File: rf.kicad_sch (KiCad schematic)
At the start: 57 parts, among them Q1 2N7002, U12 SN74AUP1G17, U13 ST25R3916B-AQET, Y3 27.12MHz

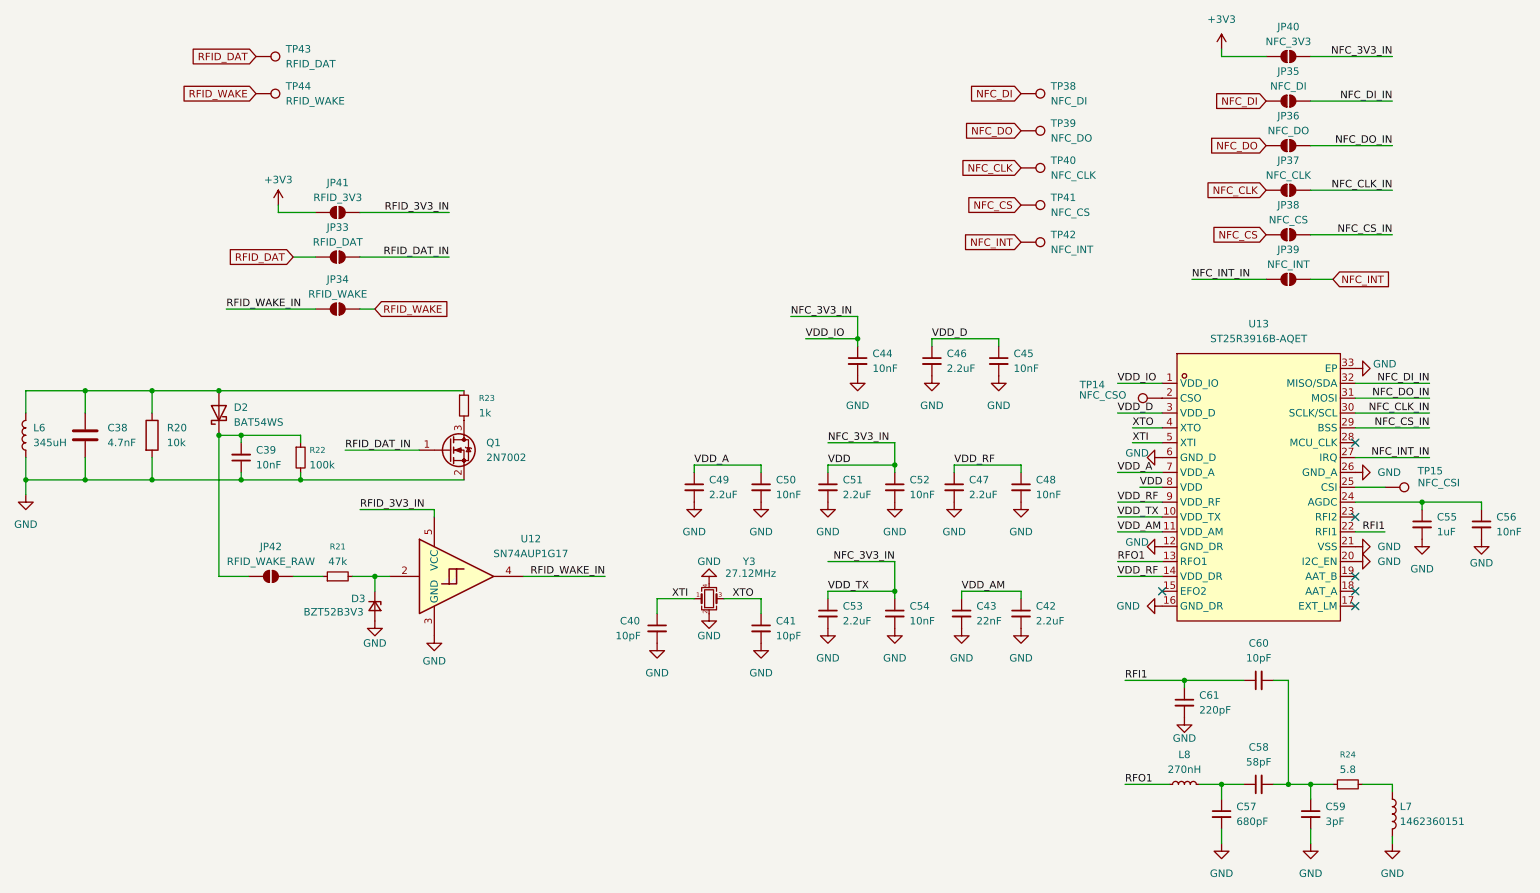
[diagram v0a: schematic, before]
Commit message: remove all jumpers
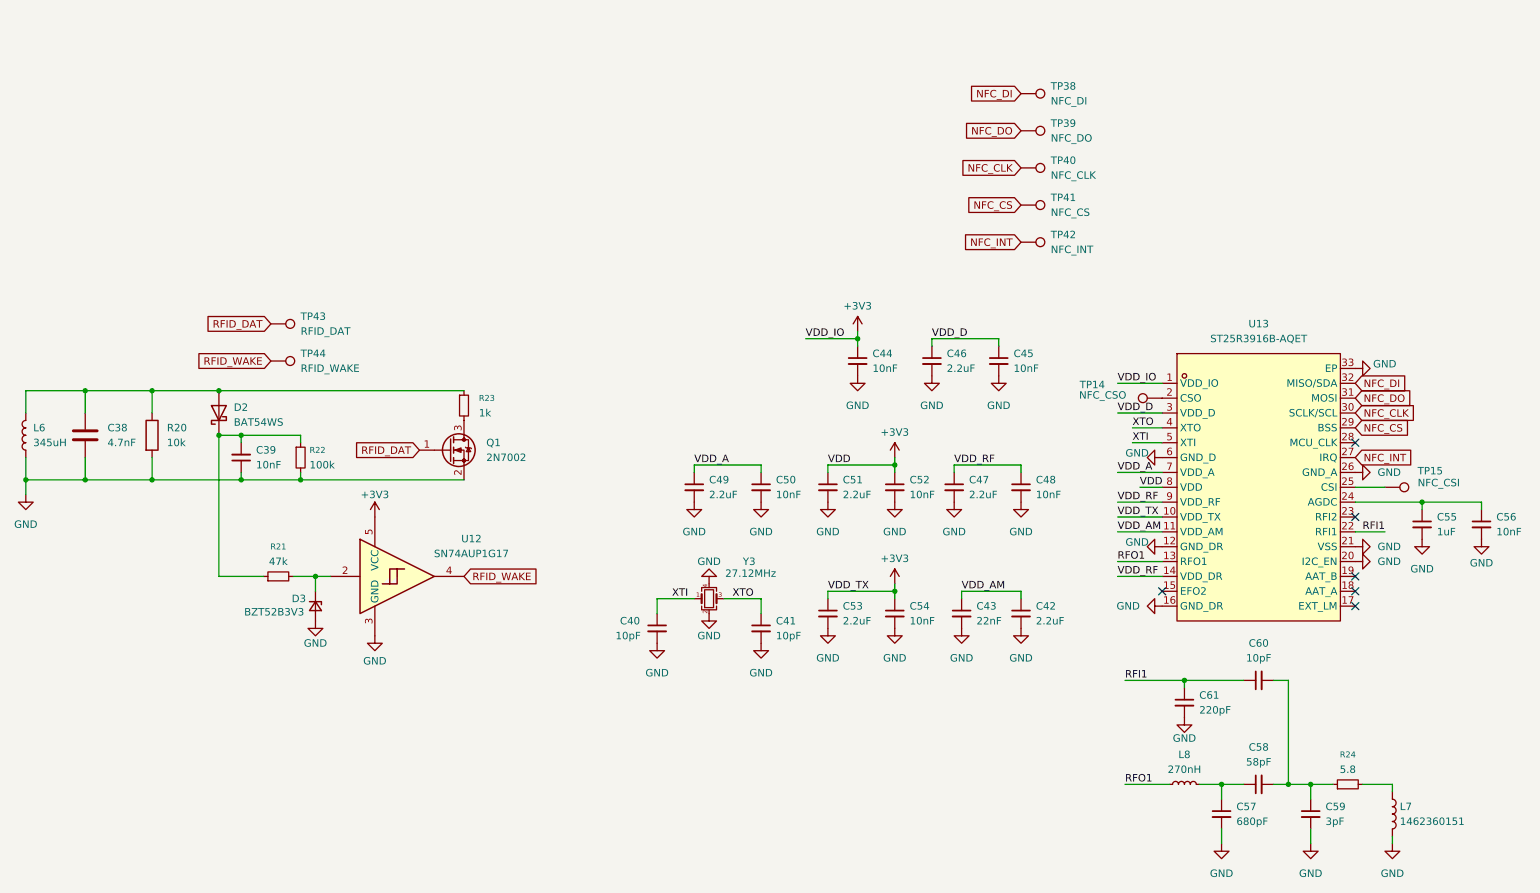
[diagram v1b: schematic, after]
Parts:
- removed JP33: RFID_DAT, Jumper:SolderJumper-2_P1.3mm_Open_Pad1.0x1.5mm, symbol Jumper:SolderJumper_2_Open
- removed JP34: RFID_WAKE, Jumper:SolderJumper-2_P1.3mm_Open_Pad1.0x1.5mm, symbol Jumper:SolderJumper_2_Open
- removed JP35: NFC_DI, Jumper:SolderJumper-2_P1.3mm_Open_Pad1.0x1.5mm, symbol Jumper:SolderJumper_2_Open
- removed JP36: NFC_DO, Jumper:SolderJumper-2_P1.3mm_Open_Pad1.0x1.5mm, symbol Jumper:SolderJumper_2_Open
- removed JP37: NFC_CLK, Jumper:SolderJumper-2_P1.3mm_Open_Pad1.0x1.5mm, symbol Jumper:SolderJumper_2_Open
- removed JP38: NFC_CS, Jumper:SolderJumper-2_P1.3mm_Open_Pad1.0x1.5mm, symbol Jumper:SolderJumper_2_Open
- removed JP39: NFC_INT, Jumper:SolderJumper-2_P1.3mm_Open_Pad1.0x1.5mm, symbol Jumper:SolderJumper_2_Open
- removed JP40: NFC_3V3, Jumper:SolderJumper-2_P1.3mm_Open_Pad1.0x1.5mm, symbol Jumper:SolderJumper_2_Open
- removed JP41: RFID_3V3, Jumper:SolderJumper-2_P1.3mm_Open_Pad1.0x1.5mm, symbol Jumper:SolderJumper_2_Open
- removed JP42: RFID_WAKE_RAW, Jumper:SolderJumper-2_P1.3mm_Open_Pad1.0x1.5mm, symbol Jumper:SolderJumper_2_Open
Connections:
- net NFC_3V3_IN is gone; now on net +3V3: C44.1, C51.1, C52.1, C53.1, C54.1, U13.1 (VDD_IO), U13.10 (VDD_TX), U13.8 (VDD)
- net NFC_CLK_IN is gone; now on net NFC_CLK: U13.30 (SCLK/SCL)
- net NFC_CS_IN is gone; now on net NFC_CS: U13.29 (BSS)
- net NFC_DI_IN is gone; now on net NFC_DI: U13.32 (MISO/SDA)
- net NFC_DO_IN is gone; now on net NFC_DO: U13.31 (MOSI)
- net NFC_INT_IN is gone; now on net NFC_INT: U13.27 (IRQ)
- net RFID_3V3_IN is gone; now on net +3V3: U12.5 (VCC)
- net RFID_DAT_IN is gone; now on net RFID_DAT: Q1.1 (G)
- net RFID_WAKE_IN is gone; now on net RFID_WAKE: U12.4
- net at C39.2, D2.1 (K), R22.1: now also R21.1
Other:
- moved on the sheet: D3, R21, TP43, TP44, U12

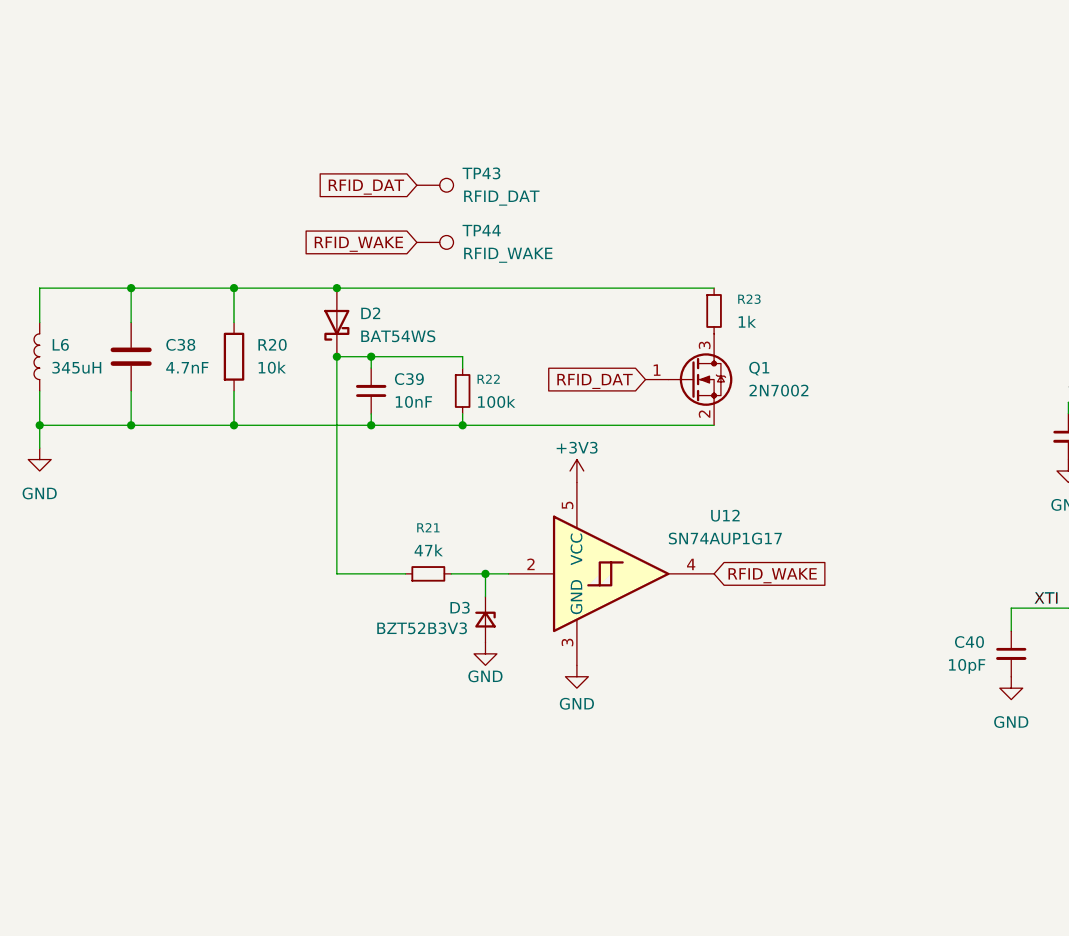
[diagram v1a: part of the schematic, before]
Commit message: revise some decoupling caps to be 0201
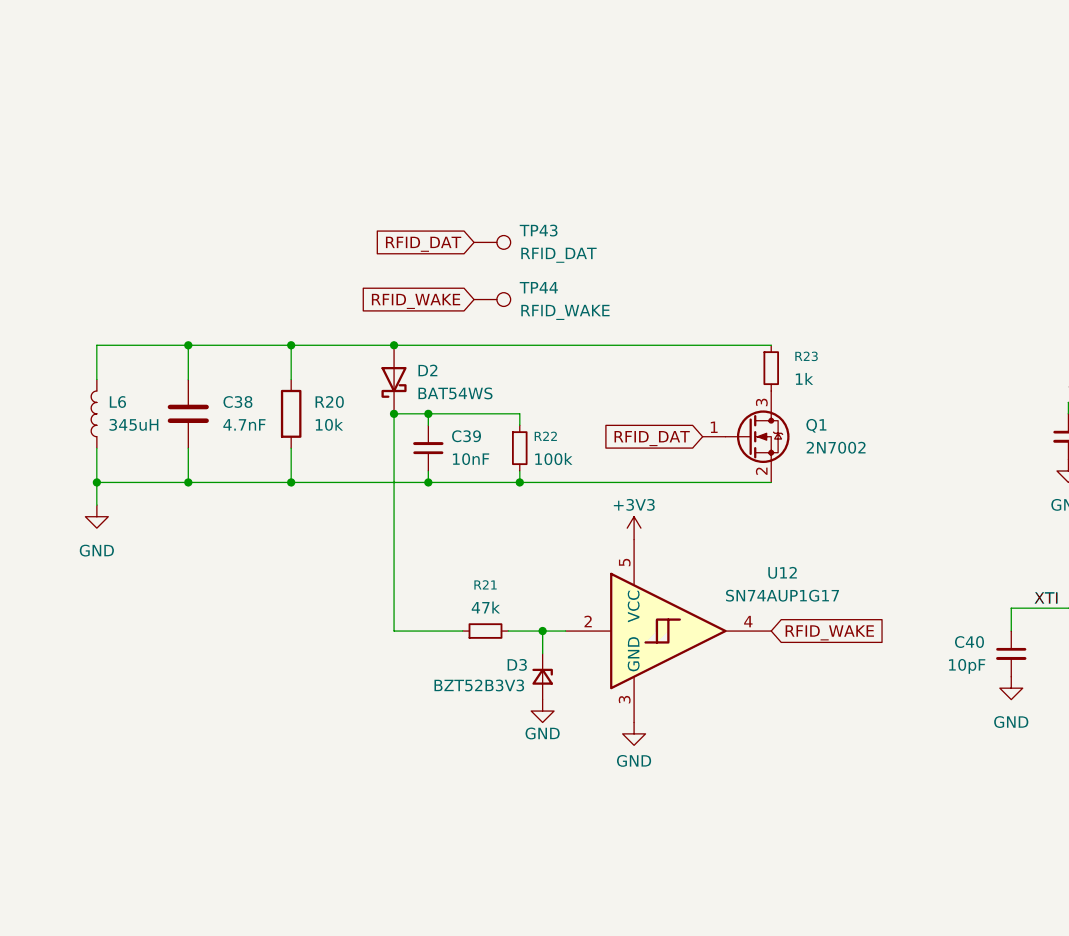
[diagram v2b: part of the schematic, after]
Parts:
- C42, C46, C47, C49, C51, C53: footprint Capacitor_SMD:C_0402_1005Metric -> Capacitor_SMD:C_0201_0603Metric; LCSC Part C1559 -> C77762
- C43: footprint Capacitor_SMD:C_0402_1005Metric -> Capacitor_SMD:C_0201_0603Metric; LCSC Part C1532 -> C668343
- C44, C45, C48, C50, C52, C54, C56: footprint Capacitor_SMD:C_0402_1005Metric -> Capacitor_SMD:C_0201_0603Metric; LCSC Part C15195 -> C85930
- C55: footprint Capacitor_SMD:C_0402_1005Metric -> Capacitor_SMD:C_0201_0603Metric; LCSC Part C52923 -> C53067
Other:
- moved on the sheet: C38, C39, D2, D3, L6, Q1, R20, R21, R22, R23, TP43, TP44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

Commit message: layout progress
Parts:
- removed TP38: NFC_DI, TestPoint:TestPoint_Pad_D1.0mm, symbol Connector:TestPoint
- removed TP39: NFC_DO, TestPoint:TestPoint_Pad_D1.0mm, symbol Connector:TestPoint
- removed TP40: NFC_CLK, TestPoint:TestPoint_Pad_D1.0mm, symbol Connector:TestPoint
- removed TP41: NFC_CS, TestPoint:TestPoint_Pad_D1.0mm, symbol Connector:TestPoint
- removed TP42: NFC_INT, TestPoint:TestPoint_Pad_D1.0mm, symbol Connector:TestPoint
- removed TP43: RFID_DAT, TestPoint:TestPoint_Pad_D1.0mm, symbol Connector:TestPoint
- removed TP44: RFID_WAKE, TestPoint:TestPoint_Pad_D1.0mm, symbol Connector:TestPoint

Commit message: progress 2
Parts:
- D2: value BAT54WS -> RB521S30T1G; footprint Diode_SMD:D_SOD-323F -> Diode_SMD:D_SOD-523; LCSC Part C7502694 -> C145179
- D3: value BZT52B3V3 -> BZX584C3V3; footprint Diode_SMD:D_SOD-123 -> Diode_SMD:D_SOD-523; LCSC Part C19077392 -> C19077462
- Q1: value 2N7002 -> 2N7002T; footprint Package_TO_SOT_SMD:SOT-23 -> Package_TO_SOT_SMD:SOT-523; LCSC Part C8545 -> C2844731
- R23: footprint Resistor_SMD:R_0603_1608Metric -> Resistor_SMD:R_0402_1005Metric; LCSC Part C21190 -> C11702
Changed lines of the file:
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@@
 			)
 		)
-		(property "Value" "BZT52B3V3"
+		(property "Value" "BZX584C3V3"
 			(at 64.008 124.206 90)
 			(effects
@@
 			)
 		)
-		(property "Footprint" "Diode_SMD:D_SOD-123"
+		(property "Footprint" "Diode_SMD:D_SOD-523"
 			(at 76.2 123.19 90)
 			(effects
@@
 			)
 		)
-		(property "LCSC Part" "C19077392"
+		(property "LCSC Part" "C19077462"
 			(at 76.2 123.19 90)
 			(effects
@@
 			)
 		)
-		(property "Footprint" "Resistor_SMD:R_0603_1608Metric"
+		(property "Footprint" "Resistor_SMD:R_0402_1005Metric"
 			(at 101.6 88.9 0)
 			(effects
@@
 			)
 		)
-		(property "LCSC Part" "C21190"
+		(property "LCSC Part" "C11702"
 			(at 101.6 88.9 0)
 			(effects
@@
 			)
 		)
-		(property "Value" "BAT54WS"
+		(property "Value" "RB521S30T1G"
 			(at 62.23 91.7574 90)
 			(effects
@@
 			)
 		)
-		(property "Footprint" "Diode_SMD:D_SOD-323F"
+		(property "Footprint" "Diode_SMD:D_SOD-523"
 			(at 59.69 90.17 0)
 			(effects
@@
 			)
 		)
-		(property "LCSC Part" "C7502694"
+		(property "LCSC Part" "C145179"
 			(at 59.69 90.17 90)
 			(effects
@@
 			)
 		)
-		(property "Value" "2N7002"
+		(property "Value" "2N7002T"
 			(at 105.41 97.7899 0)
 			(effects
@@
 			)
 		)
-		(property "Footprint" "Package_TO_SOT_SMD:SOT-23"
+		(property "Footprint" "Package_TO_SOT_SMD:SOT-523"
 			(at 104.14 98.425 0)
 			(effects
@@
 			)
 		)
-		(property "LCSC Part" "C8545"
+		(property "LCSC Part" "C2844731"
 			(at 99.06 96.52 0)
 			(effects

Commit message: huge progress
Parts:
- removed TP14: NFC_CSO, TestPoint:TestPoint_Pad_D1.0mm, symbol Connector:TestPoint
- removed TP15: NFC_CSI, TestPoint:TestPoint_Pad_D1.0mm, symbol Connector:TestPoint
- L7: value 1462360151 -> FXC.16.A.DG
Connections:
- no-connect marks 6 -> 8

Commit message: final fixups before prod
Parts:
- C36: renamed from C49; LCSC Part C77762 -> C335106
- C37: renamed from C50; LCSC Part C85930 -> C272853
- C39: renamed from C51; LCSC Part C77762 -> C335106
- C40: renamed from C53; LCSC Part C77762 -> C335106
- C41: renamed from C44; LCSC Part C85930 -> C272853
- C42: renamed from C52; LCSC Part C85930 -> C272853
- C43: renamed from C54; LCSC Part C85930 -> C272853
- C44: renamed from C46; LCSC Part C77762 -> C335106
- C45: renamed from C47; LCSC Part C77762 -> C335106
- C47: renamed from C45; LCSC Part C85930 -> C272853
- C48, C56: LCSC Part C85930 -> C272853
- C49: renamed from C42; LCSC Part C77762 -> C335106
- C50: renamed from C61; LCSC Part C1530 -> C71693
- C53: renamed from C58; value 58pF -> 90pF; LCSC Part C526981 -> C1864488
- C54: renamed from C59; value 3pF -> 53pF; LCSC Part C1564 -> C541437
- R24: value 5.8 -> 2.02; LCSC Part C423151 -> C2998051
- U13: value ST25R3916B-AQET -> ST25R3918-AQWT; LCSC Part C17315217 -> C3304617
- renumbered C38 to C33, C39 to C34, C40 to C35, C41 to C38, C43 to C46, C57 to C51, C60 to C52, D2 to D4, D3 to D5, L8 to L7, L7 to L8
